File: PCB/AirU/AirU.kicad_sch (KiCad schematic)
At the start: 0 parts

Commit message: setup parts libraries
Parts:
- added C?: 0.1uF, symbol Device:C
- added H1: 2894, 2984:2894, symbol 2894:2894
- added IC1: LD1086DT50TR, LD1086DT50TR:LD1086DT33TR, symbol LD1086DT50TR:LD1086DT50TR
- added IC2: L70B-M39, L70B-M39:L76, symbol L70B-M39:L70B-M39
- added IC3: NCV21872DR2G, NCV21872DR2G:SOIC127P600X175-8N, symbol NCV21872DR2G:NCV21872DR2G
- added J1: MEM2051-00-195-00-A, MEM2051-00-195-00-A:MEM20510019500A, symbol MEM2051-00-195-00-A:MEM2051-00-195-00-A
- added J2: ZX62-B-5PA_33_, ZX62-B-5PA_33_:ZX62B5PA33, symbol ZX62-B-5PA_33_:ZX62-B-5PA_33_
- added J3: 53261-7008, 53261-7008:532617008, symbol 53261-7008:53261-7008
- added Q1, Q2: MMBT3904, Package_TO_SOT_SMD:SOT-23, symbol Transistor_BJT:MMBT3904
- added R1, R2, R3: R, symbol Device:R
- added U1: ESP32-S3-WROOM-1, Espressif:ESP32-S3-WROOM-1, symbol Espressif:ESP32-S3-WROOM-1
- added U2: CH340E, Package_SO:MSOP-10_3x3mm_P0.5mm, symbol Interface_USB:CH340E
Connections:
- new net D+: U2.1 (UD+)
- new net D-: U2.2 (UD-)
- new net EN: U1.3 (EN)
- new net GND: C?.2, U1.1 (GND), U1.40 (GND), U1.41 (GND), U2.3 (GND)
- new net GPIO0: U1.27 (GPIO0/BOOT)
- new net GPIO1: U1.39 (GPIO1/TOUCH1/ADC1_CH0)
- new net GPIO10: U1.18 (GPIO10/TOUCH10/ADC1_CH9/FSPICS0/FSPIIO4/SUBSPICS0)
- new net GPIO11: U1.19 (GPIO11/TOUCH11/ADC2_CH0/FSPID/FSPIIO5/SUBSPID)
- new net GPIO12: U1.20 (GPIO12/TOUCH12/ADC2_CH1/FSPICLK/FSPIIO6/SUBSPICLK)
- new net GPIO13: U1.21 (GPIO13/TOUCH13/ADC2_CH2/FSPIQ/FSPIIO7/SUBSPIQ)
- new net GPIO14: U1.22 (GPIO14/TOUCH14/ADC2_CH3/FSPIWP/FSPIDQS/SUBSPIWP)
- new net GPIO15: U1.8 (GPIO15/U0RTS/ADC2_CH4/XTAL_32K_P)
- new net GPIO16: U1.9 (GPIO16/U0CTS/ADC2_CH5/XTAL_32K_NH5)
- new net GPIO17: U1.10 (GPIO17/U1TXD/ADC2_CH6)
- new net GPIO18: U1.11 (GPIO18/U1RXD/ADC2_CH7/CLK_OUT3)
- new net GPIO19: U1.13 (GPIO19/U1RTS/ADC2_CH8/CLK_OUT2/USB_D-)
- new net GPIO2: U1.38 (GPIO2/TOUCH2/ADC1_CH1)
- new net GPIO20: U1.14 (GPIO20/U1CTS/ADC2_CH9/CLK_OUT1/USB_D+)
- new net GPIO21: U1.23 (GPIO21)
- new net GPIO3: U1.15 (GPIO3/TOUCH3/ADC1_CH2)
- new net GPIO35: U1.28 (SPIIO6/GPIO35/FSPID/SUBSPID)
- new net GPIO36: U1.29 (SPIIO7/GPIO36/FSPICLK/SUBSPICLK)
- new net GPIO37: U1.30 (SPIDQS/GPIO37/FSPIQ/SUBSPIQ)
- new net GPIO38: U1.31 (GPIO38/FSPIWP/SUBSPIWP)
- new net GPIO39: U1.32 (MTCK/GPIO39/CLK_OUT3/SUBSPICS1)
- new net GPIO4: U1.4 (GPIO4/TOUCH4/ADC1_CH3)
- new net GPIO40: U1.33 (MTDO/GPIO40/CLK_OUT2)
- new net GPIO41: U1.34 (MTDI/GPIO41/CLK_OUT1)
- new net GPIO42: U1.35 (MTMS/GPIO42)
- new net GPIO45: U1.26 (GPIO45)
- new net GPIO46: U1.16 (GPIO46)
- new net GPIO47: U1.24 (GPIO47/SPICLK_P/SUBSPICLK_P_DIFF)
- new net GPIO48: U1.25 (GPIO48/SPICLK_N/SUBSPICLK_N_DIFF)
- new net GPIO5: U1.5 (GPIO5/TOUCH5/ADC1_CH4)
- new net GPIO6: U1.6 (GPIO6/TOUCH6/ADC1_CH5)
- new net GPIO7: U1.7 (GPIO7/TOUCH7/ADC1_CH6)
- new net GPIO8: U1.12 (GPIO8/TOUCH8/ADC1_CH7/SUBSPICS1)
- new net GPIO9: U1.17 (GPIO9/TOUCH9/ADC1_CH8/FSPIHD/SUBSPIHD)
- new net U0RXD: U1.36 (U0RXD/GPIO44/CLK_OUT2)
- new net U0TXD: U1.37 (U0TXD/GPIO43/CLK_OUT1)
- new net VDD: C?.1, U1.2 (3V3), U2.10 (V3), U2.7 (VCC)
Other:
- note added: "ESP32 Connections"
- note added: "Important Notes Vdd : 3.3V Vcc : 5V"
- title: (none) -> AirU

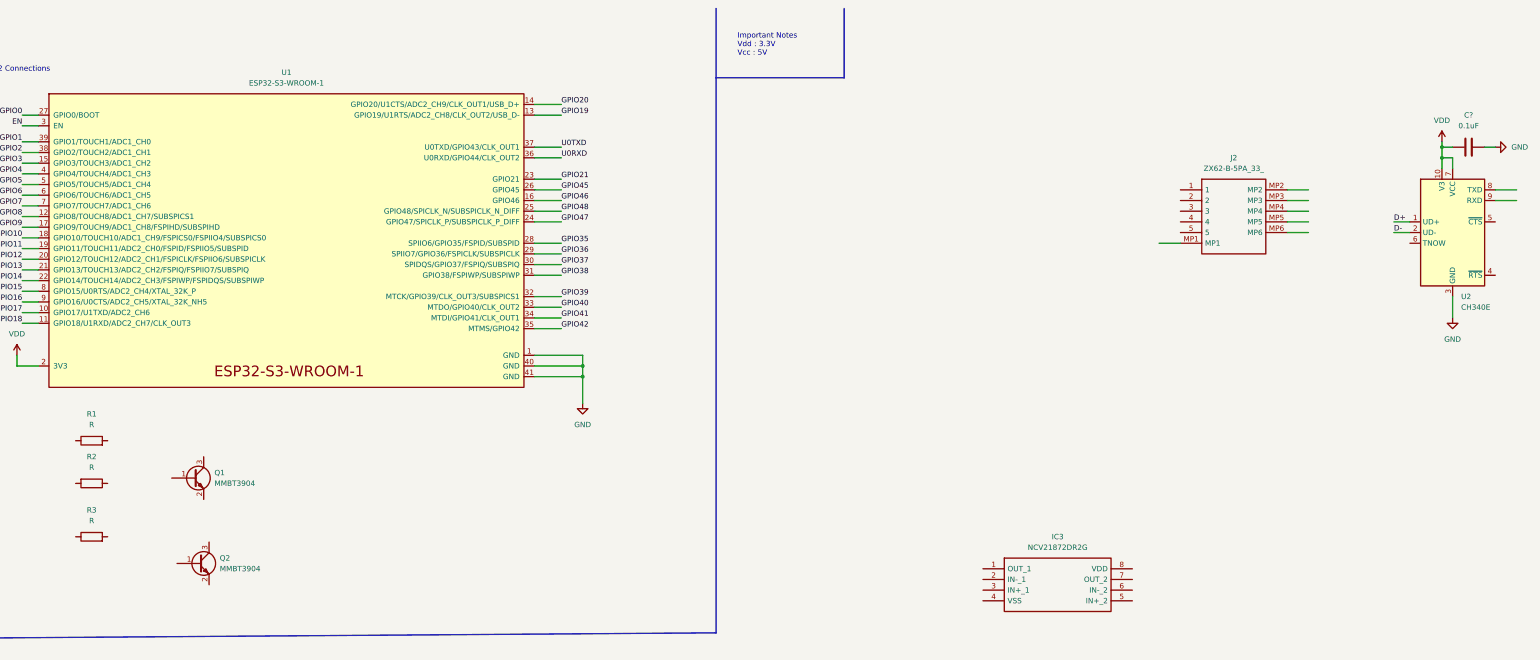
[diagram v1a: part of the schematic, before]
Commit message: usb to serial done on schematic
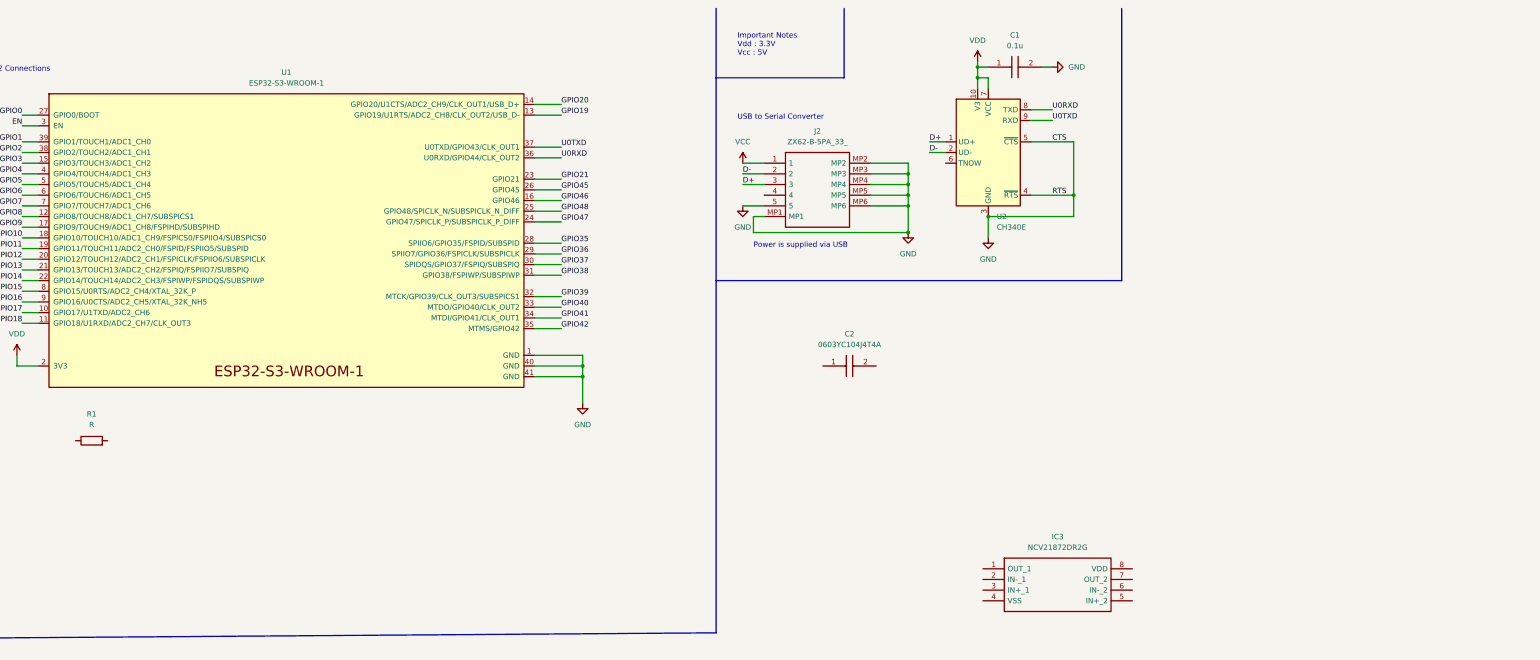
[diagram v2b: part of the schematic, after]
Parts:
- removed C?: 0.1uF, symbol Device:C
- removed Q1, Q2: MMBT3904, Package_TO_SOT_SMD:SOT-23, symbol Transistor_BJT:MMBT3904
- removed R2, R3: R, symbol Device:R
- added C1: 0.1u, 0603YC104J4T4A:CAPC1608X90N, symbol 0603YC104J4T4A:0603YC104J4T4A
- added C2: 0603YC104J4T4A, 0603YC104J4T4A:CAPC1608X90N, symbol 0603YC104J4T4A:0603YC104J4T4A
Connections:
- net D+: now also J2.3
- net D-: now also J2.2
- net GND: now also J2.5, J2.MP1, J2.MP2, J2.MP3, J2.MP4, J2.MP5, J2.MP6, U2.4 (~{RTS}), U2.5 (~{CTS}), C1.2
- net U0RXD: now also U2.8 (TXD)
- net U0TXD: now also U2.9 (RXD)
- net VDD: now also C1.1
- net VCC: now reaches J2.1
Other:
- note added: "Power is supplied via USB"
- note added: "USB to Serial Converter"
- moved on the sheet: J2, U2

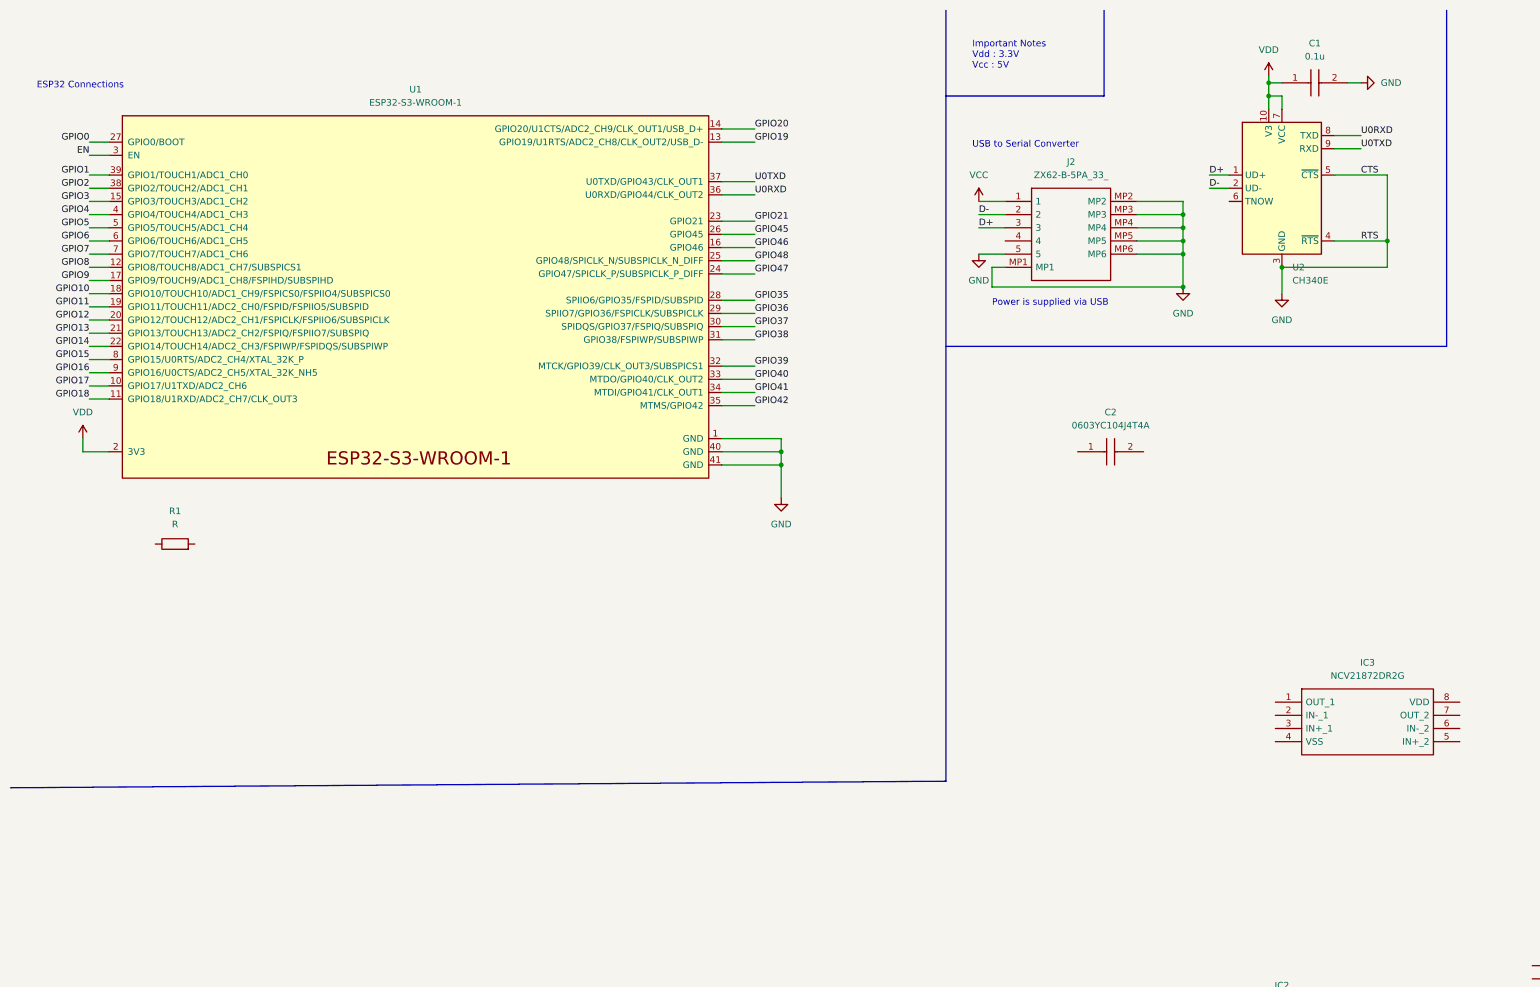
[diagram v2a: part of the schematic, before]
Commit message: added footprint for lora breakout board
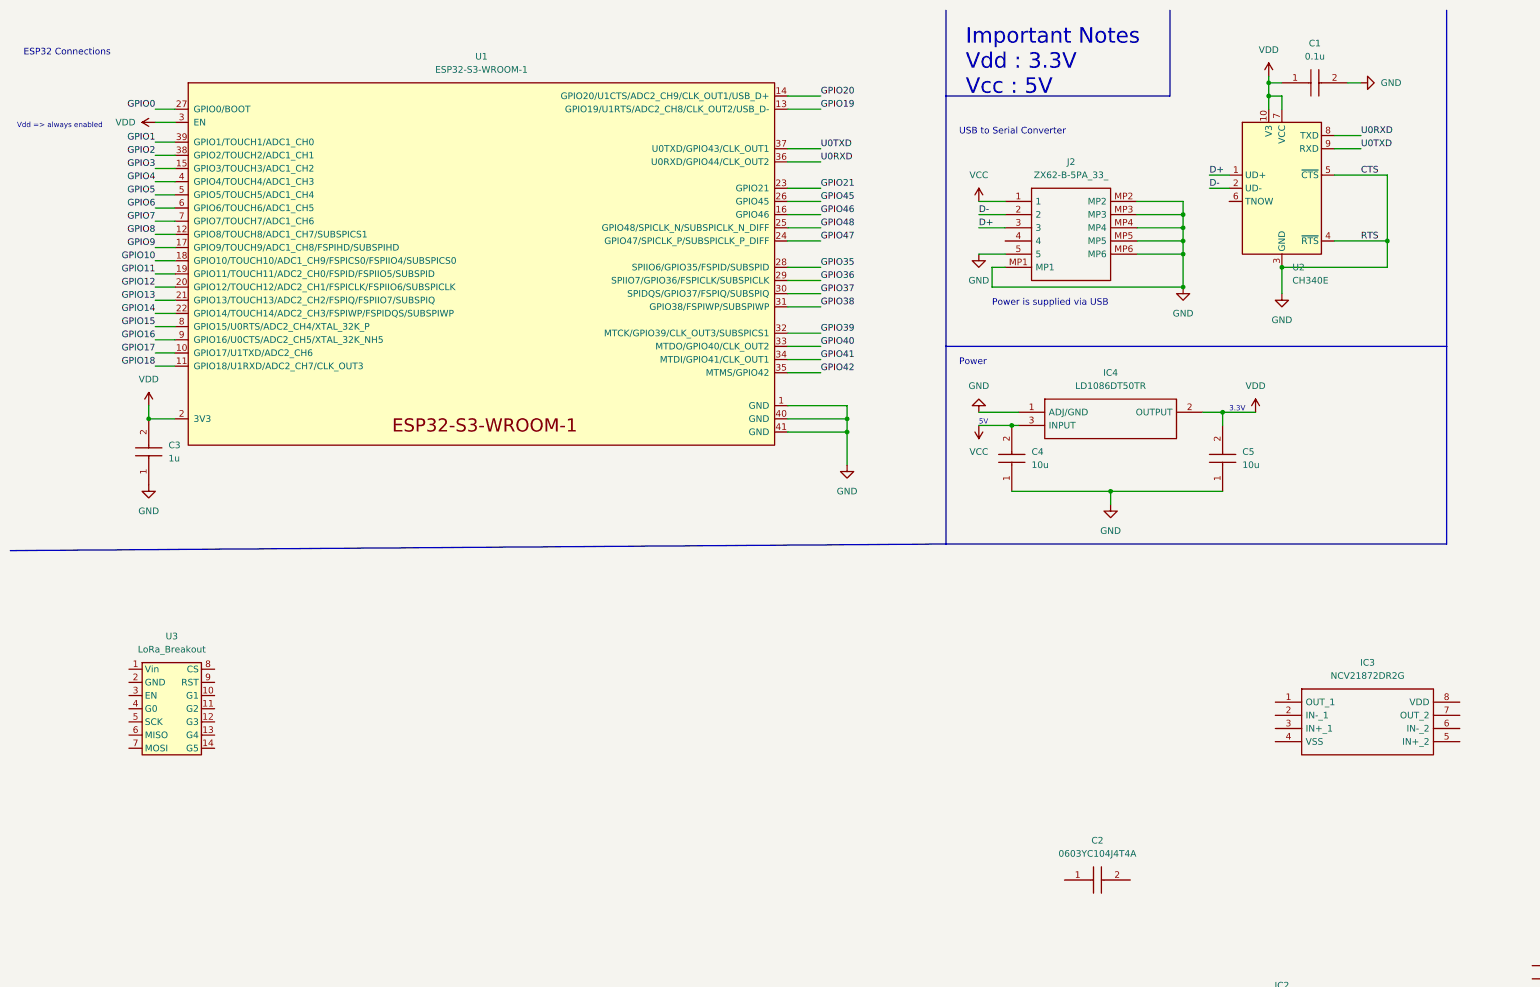
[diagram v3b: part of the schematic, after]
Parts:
- removed R1: R, symbol Device:R
- added C3: 1u, 0603YC105KAT2A:CAPC1608X94N, symbol 0603YC105KAT2A:0603YC105KAT2A
- added C4, C5: 10u, 0603ZDD106KAT2A:CAPC1608X90N, symbol 0603ZD106KAT2A:0603ZD106KAT2A
- added IC4: LD1086DT50TR, LD1086DT50TR:LD1086DT33TR, symbol LD1086DT50TR:LD1086DT50TR
- added U3: LoRa_Breakout, custom_components:LoRa_Breakout, symbol custom_components:LoRa_Breakout
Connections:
- net EN is gone; now on net VDD: U1.3 (EN)
- net GND: now also C3.1, C4.1, C5.1, IC4.1 (ADJ/GND)
- net VCC: now also C4.2, IC4.3 (INPUT)
- net VDD: now also C3.2, C5.2, IC4.2 (OUTPUT)
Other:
- note added: "3.3V"
- note added: "5V"
- note added: "Power"
- note added: "Vdd => always enabled"
- moved on the sheet: C2, U1

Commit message: added most parts to pcb
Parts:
- removed C2: 0603YC104J4T4A, 0603YC104J4T4A:CAPC1608X90N, symbol 0603YC104J4T4A:0603YC104J4T4A
- removed H1: 2894, 2984:2894, symbol 2894:2894
- removed IC1: LD1086DT50TR, LD1086DT50TR:LD1086DT33TR, symbol LD1086DT50TR:LD1086DT50TR
- removed IC2: L70B-M39, L70B-M39:L76, symbol L70B-M39:L70B-M39
- removed IC3: NCV21872DR2G, NCV21872DR2G:SOIC127P600X175-8N, symbol NCV21872DR2G:NCV21872DR2G
- removed J1: MEM2051-00-195-00-A, MEM2051-00-195-00-A:MEM20510019500A, symbol MEM2051-00-195-00-A:MEM2051-00-195-00-A
- removed J3: 53261-7008, 53261-7008:532617008, symbol 53261-7008:53261-7008
- added D1: LED, LED_SMD:LED_0603_1608Metric, symbol Device:LED
- added J1: 53261-7008, 53261-7008:532617008, symbol 53261-7008:53261-7008
- added R1, R10, R11, R2, R3, R4, R5, R6, R7, R8, R9: 0, Resistor_SMD:R_0603_1608Metric, symbol Device:R
- added R12: 820, Resistor_SMD:R_0603_1608Metric, symbol Device:R
- added R13: 130, Resistor_SMD:R_0603_1608Metric, symbol Device:R
- added R14: 27, Resistor_SMD:R_0603_1608Metric, symbol Device:R
- added U4: MICS6814, chem_air_u_footprints:PLCC125P750X550X150-16N, symbol custom_components:MICS6814
- C1: renamed from C3; value 1u -> 0603YC105KAT2A
- renumbered C4 to C2, C5 to C4, C1 to C5, IC4 to IC3
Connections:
- net GND: now also U3.2 (GND), D1.1 (K), J1.MP1, J1.MP2, U4.2 (B), U4.6 (F), U4.9 (J)
- net GPIO10: now also U4.1 (A)
- net GPIO12: now also R4.2
- net GPIO13: now also R3.2
- net GPIO14: now also R2.2, R9.2
- net GPIO15: now also R5.2
- net GPIO17: now also R10.2
- net GPIO18: now also R11.2
- net GPIO4: now also R8.2
- net GPIO5: now also R1.2
- net GPIO6: now also R7.2
- net GPIO7: now also R6.2
- net GPIO9: now also U4.4 (D)
- net VCC: now also R12.2, R13.1, R14.2
- net VDD: now also U3.1 (Vin), U3.3 (EN)
- net LORA_DIO1: now reaches U3.10 (G1)
- net LORA_DIO1: now also R7.1
- net LORA_DIO2: now reaches U3.11 (G2)
- net LORA_DIO2: now also R8.1
- net LORA_DIO3: now reaches U3.12 (G3)
- net LORA_DIO3: now also R9.1
- net LORA_DIO4: now reaches U3.13 (G4)
- net LORA_DIO4: now also R10.1
- net LORA_DIO5: now reaches U3.14 (G5)
- net LORA_DIO5: now also R11.1
- net LORA_DIO0: now reaches U3.4 (G0)
- net LORA_DIO0: now also R1.1
- net LORA_SCLK: now reaches U3.5 (SCK)
- net LORA_SCLK: now also R2.1
- net LORA_MISO: now reaches U3.6 (MISO)
- net LORA_MISO: now also R3.1
- net LORA_MOSI: now reaches U3.7 (MOSI)
- net LORA_MOSI: now also R4.1
- net LORA_NSS: now reaches U3.8 (CS)
- net LORA_NSS: now also R5.1
- net LORA_RST: now reaches U3.9 (RST)
- net LORA_RST: now also R6.1
- net at U2.6 (TNOW): now also D1.2 (A)
- net GPIO8 renamed CO_VALUE
- net CO_VALUE: now also U4.8 (H)
- new net: R13.2, U4.10 (K)
- new net: R14.1, U4.3 (C)
- new net: R12.1, U4.5 (E), U4.7 (G)
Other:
- note added: "LED indicates when transmission occurs."
- note added: "LoRa Breakout Board"
- note added: "MICS 6814: NH3, NO2, CO Sensor"
- note added: "MOLEX Connector"
- note added: "Pin Connections (note needs ADC on the ESP32): CO_VALUE: GPIO8 NH3_VALUE: GPIO9 NO2_VALUE: GPIO10"
- note added: "Pin Connections in Code: RESET: GPIO7 MOSI: GPIO12 MISO: GPIO13 SCLK: GPIO14 NSS: GPIO15 DIO0: GPIO5 DIO1: GPIO6 Additional Connections on PCB in case necessary: DIO2: GPIO4 DIO3: GPIO16 DIO4: GPIO17 DIO5: GPIO18"
- note added: "Vcc is supplied from the USB connection."
- moved on the sheet: U3

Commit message: schematic complete
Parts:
- added R15, R16: 3k, Resistor_SMD:R_0603_1608Metric, symbol Device:R
- added R17, R18: 10k, Resistor_SMD:R_0603_1608Metric, symbol Device:R
- added U5: HDC2010YPAR, footprints:HDC2010YPAR, symbol 2022-11-07_15-59-30:HDC2010YPAR
- C1: value 0603YC105KAT2A -> 0.1u
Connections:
- net GND: now also J1.2, U5.B1 (ADDR), U5.C1 (GND)
- net GPIO18: now also U4.8 (H), R16.2, U5.A2 (SDA)
- net GPIO19: now also R15.2, U5.B2 (SCL)
- net GPIO36: now also U5.C2 (DRDY_INT)
- net GPIO45: now also J1.3, R18.2
- net GPIO46: now also J1.6, R17.2
- net GPIO48: now also J1.5
- net VCC: now also J1.1
- net VDD: now also R15.1, R16.1, R17.1, R18.1, U5.A1 (VDD)
- net CO_VALUE renamed GPIO8
- net GPIO8: no longer U4.8 (H)
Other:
- note added: "HDC2010: Temperature and humidity sensor"
- note added: "Pin Connections: Pins 7 and 8 remain unconnected. Pin 4 (RXD) is unused in this application. TXD: GPIO48 SET: GPIO45 RESET: GPIO46"
- note added: "Pin Connections: SCL: GPIO19 SDA: GPIO18 DRDY_INT: GPIO36"
- moved on the sheet: J1
